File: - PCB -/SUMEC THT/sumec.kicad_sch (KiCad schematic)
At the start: 0 parts

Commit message: QRE Array - WIP
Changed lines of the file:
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@@
     (company "SPŠ NA PROSEKU")
-  )
-  (symbol (lib_id "Graphic:Logo_Open_Hardware_Small") (at 130.81 105.41 0) (unit 1)
-    (in_bom no) (on_board no) (dnp no) (fields_autoplaced)
-    (property "Reference" "#SYM1" (at 130.81 98.425 0)
-      (effects (font (size 1.27 1.27)) hide)
-    )
-    (property "Value" "Logo_Open_Hardware_Small" (at 130.81 111.125 0)
-      (effects (font (size 1.27 1.27)) hide)
-    )
-    (property "Footprint" "" (at 130.81 105.41 0)
-      (effects (font (size 1.27 1.27)) hide)
-    )
-    (property "Datasheet" "~" (at 130.81 105.41 0)
-      (effects (font (size 1.27 1.27)) hide)
-    )
-    (property "Sim.Enable" "0" (at 130.81 105.41 0)
-      (effects (font (size 1.27 1.27)) hide)
-    )
-    (instances
-      (project "sumec"
-        (path "/fc70a1a8-ed7c-4a0f-9b1a-f23293528385"
-          (reference "#SYM1") (unit 1)
-        )
-      )
-    )
   )
   (sheet (at 21.59 83.82) (size 69.85 46.99)

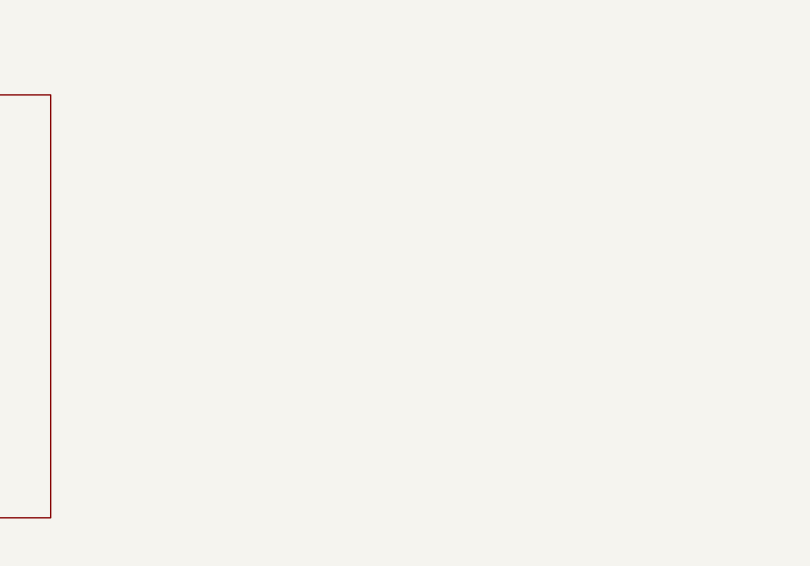
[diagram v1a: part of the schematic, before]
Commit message: Revert "Merge branch 'sumec-main' of https://github.com/menmenson/RoboCop into sumec-main"
This reverts commit dbf205ac3b02d72b1b38e86a27b286e1b118f9d4, reversing
changes made to f2387d167bca73d6a0741a06b82f65a42dfb555a.
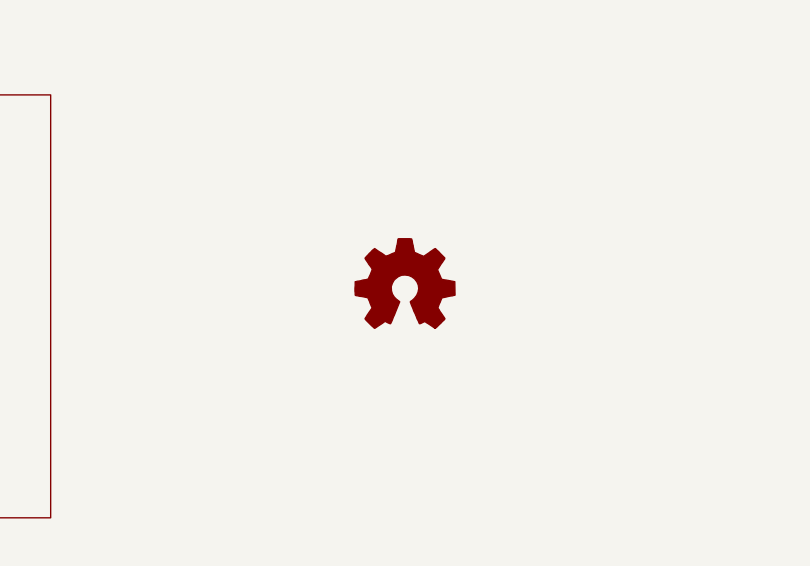
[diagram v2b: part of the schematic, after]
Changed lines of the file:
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@@
     (company "SPŠ NA PROSEKU")
+  )
+  (symbol (lib_id "Graphic:Logo_Open_Hardware_Small") (at 130.81 105.41 0) (unit 1)
+    (in_bom no) (on_board no) (dnp no) (fields_autoplaced)
+    (property "Reference" "#SYM1" (at 130.81 98.425 0)
+      (effects (font (size 1.27 1.27)) hide)
+    )
+    (property "Value" "Logo_Open_Hardware_Small" (at 130.81 111.125 0)
+      (effects (font (size 1.27 1.27)) hide)
+    )
+    (property "Footprint" "" (at 130.81 105.41 0)
+      (effects (font (size 1.27 1.27)) hide)
+    )
+    (property "Datasheet" "~" (at 130.81 105.41 0)
+      (effects (font (size 1.27 1.27)) hide)
+    )
+    (property "Sim.Enable" "0" (at 130.81 105.41 0)
+      (effects (font (size 1.27 1.27)) hide)
+    )
+    (instances
+      (project "sumec"
+        (path "/fc70a1a8-ed7c-4a0f-9b1a-f23293528385"
+          (reference "#SYM1") (unit 1)
+        )
+      )
+    )
   )
   (sheet (at 21.59 83.82) (size 69.85 46.99)
